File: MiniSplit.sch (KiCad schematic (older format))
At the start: 49 parts, among them J1 5PIN, SW1 SW_PUSH, SW10 SW_PUSH, SW11 SW_PUSH, SW12 SW_PUSH, SW13 SW_PUSH, SW14 SW_PUSH, SW15 SW_PUSH, SW16 SW_PUSH, SW17 SW_PUSH, SW18 SW_PUSH, SW19 SW_PUSH, SW2 SW_PUSH, SW20 SW_PUSH, SW21 SW_PUSH, SW3 SW_PUSH, SW4 SW_PUSH, SW5 SW_PUSH, SW6 SW_PUSH, SW7 SW_PUSH, SW8 SW_PUSH, SW9 SW_PUSH, U1 ProMicro, U2 HOLE, U3 HOLE, U4 HOLE, U5 HOLE

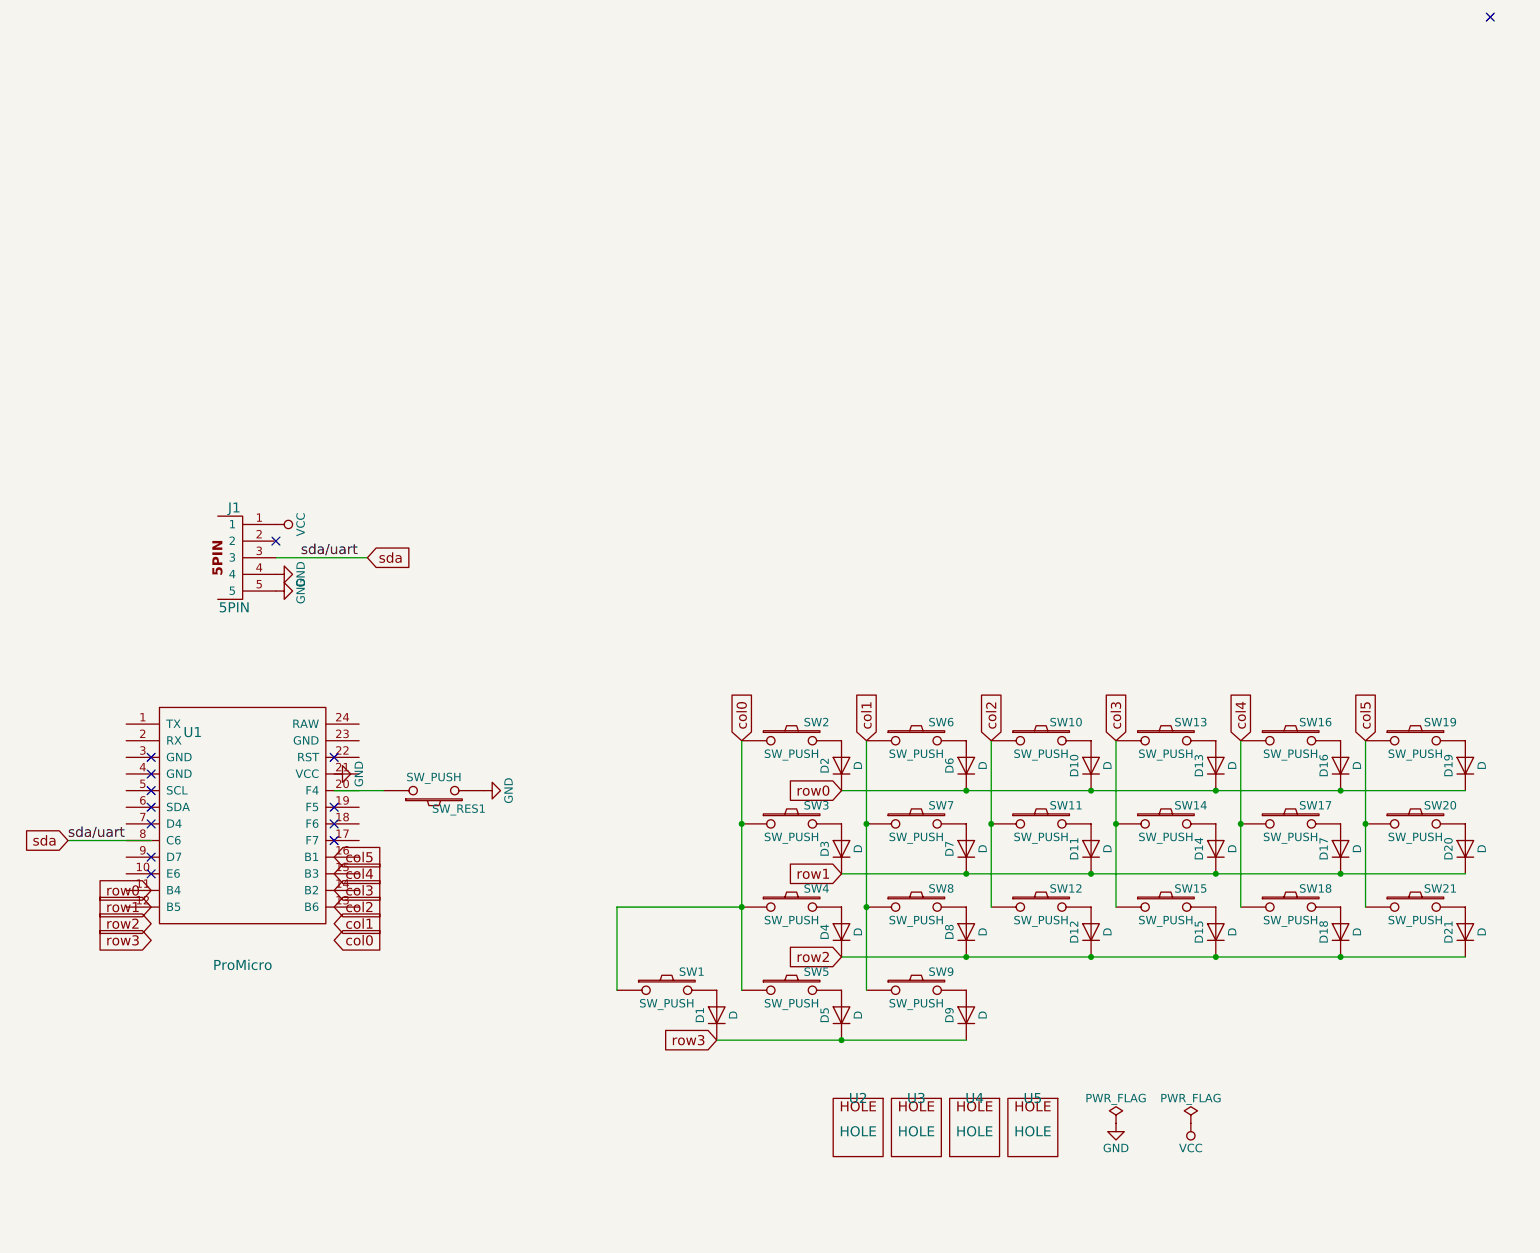
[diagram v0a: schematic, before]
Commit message: ✨ver0.2→1.0✨
42keys→50keys
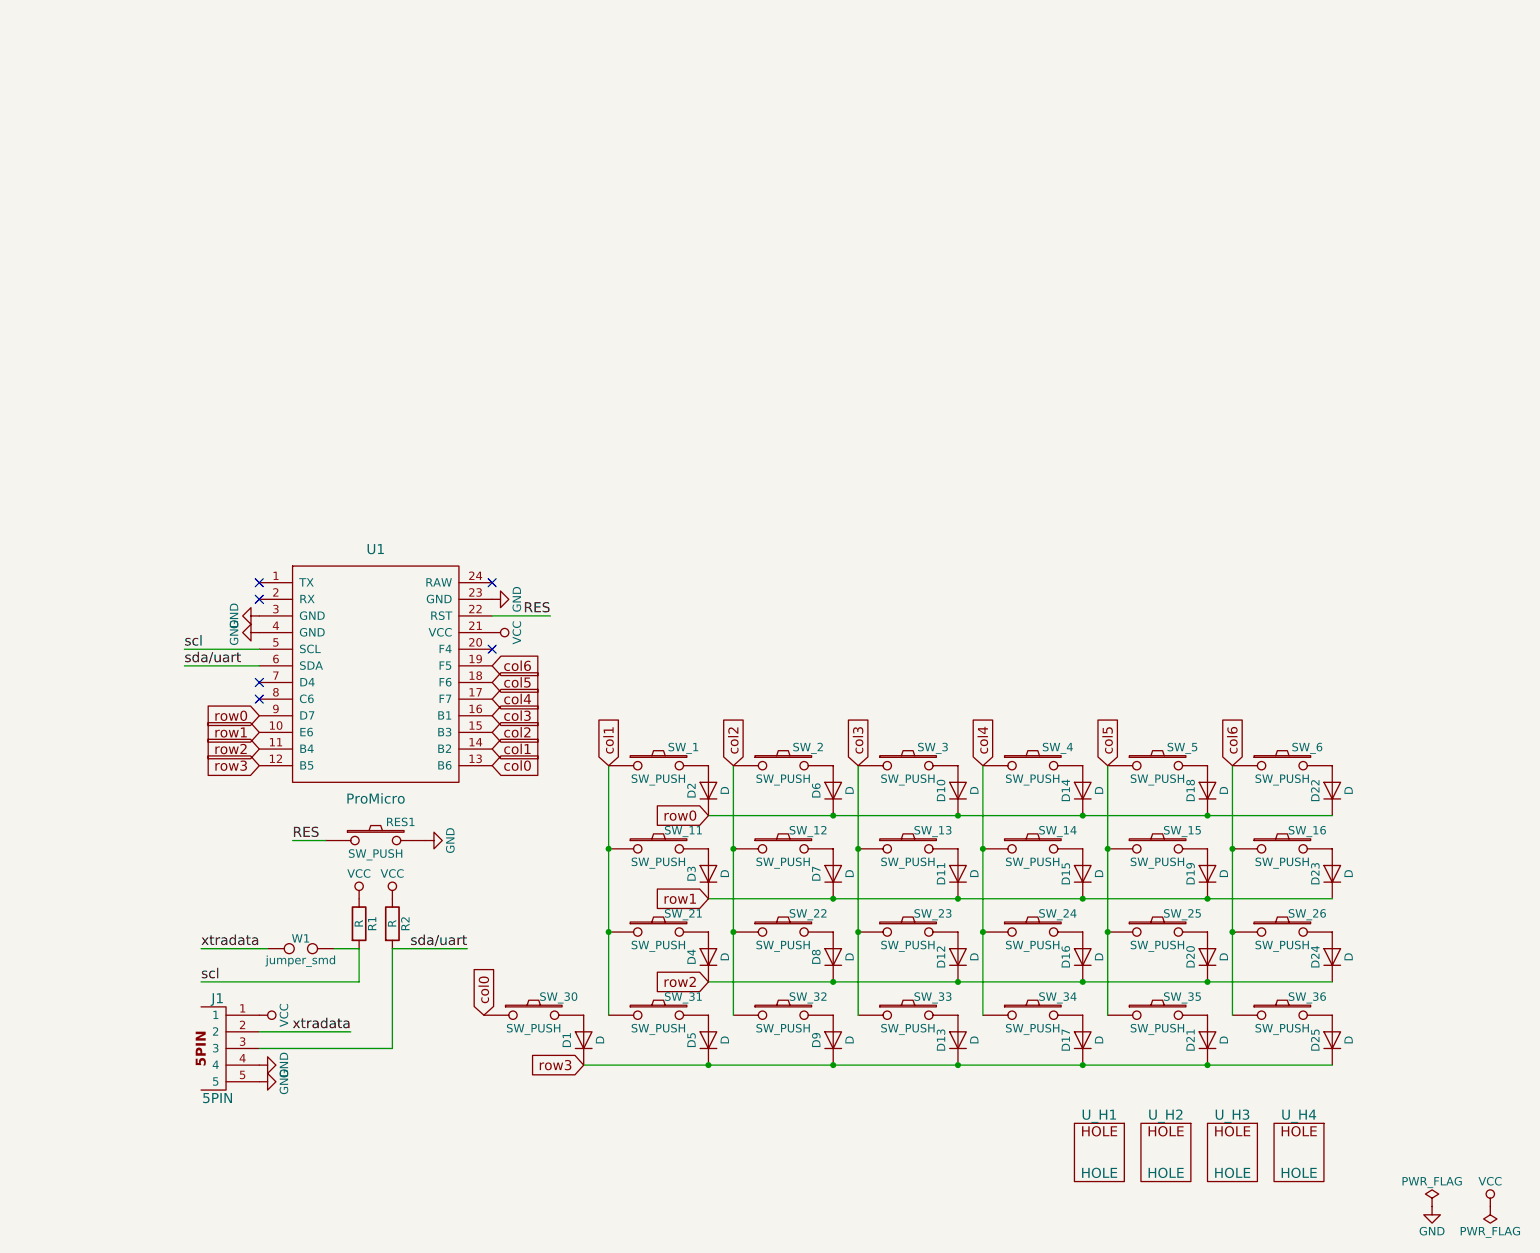
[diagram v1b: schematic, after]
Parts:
- removed SW1, SW10, SW11, SW12, SW13, SW14, SW15, SW16, SW17, SW18, SW19, SW2, SW20, SW21, SW3, SW4, SW5, SW6, SW7, SW8, SW9: SW_PUSH, lets_split-footprint:MXALPS_FLIP_HOLES, symbol SW_PUSH
- removed SW_RES1: SW_PUSH, minisplit-footprint:TACT_SWITCH_TVBP06, symbol SW_PUSH
- removed U2, U3, U4, U5: HOLE, library:hole, symbol HOLE
- added D22, D23, D24, D25: D, minisplit2-footprint:Diode_TH_SOD123, symbol D
- added R1, R2: R, promicro:RESISTOR, symbol R
- added RES1: SW_PUSH, minisplit-footprint:TACT_SWITCH_TVBP06, symbol SW_PUSH
- added SW_1, SW_11, SW_12, SW_13, SW_14, SW_15, SW_16, SW_2, SW_21, SW_22, SW_23, SW_24, SW_25, SW_26, SW_3, SW_30, SW_31, SW_32, SW_33, SW_34, SW_35, SW_36, SW_4, SW_5, SW_6: SW_PUSH, minisplit2-footprint:MX_PG1350_FLIP_HOLES, symbol SW_PUSH
- added U_H1, U_H2, U_H3, U_H4: HOLE, minisplit-footprint:hole, symbol HOLE
- added W1: jumper_smd, ergo42:jumper_smd_2dub, symbol jumper_smd
- D1, D10, D11, D12, D13, D14, D15, D16, D17, D18, D19, D2, D20, D21, D3, D4, D5, D6, D7, D8, D9: footprint footprint:Diode_TH_SOD123 -> minisplit2-footprint:Diode_TH_SOD123
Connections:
- net labels added: RES, col6, scl, xtradata
- net labels removed: sda
- wire segments 15 -> 22
- no-connect marks 13 -> 6
